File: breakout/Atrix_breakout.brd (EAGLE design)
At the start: 8.1 x 17.4 mm, 9 parts

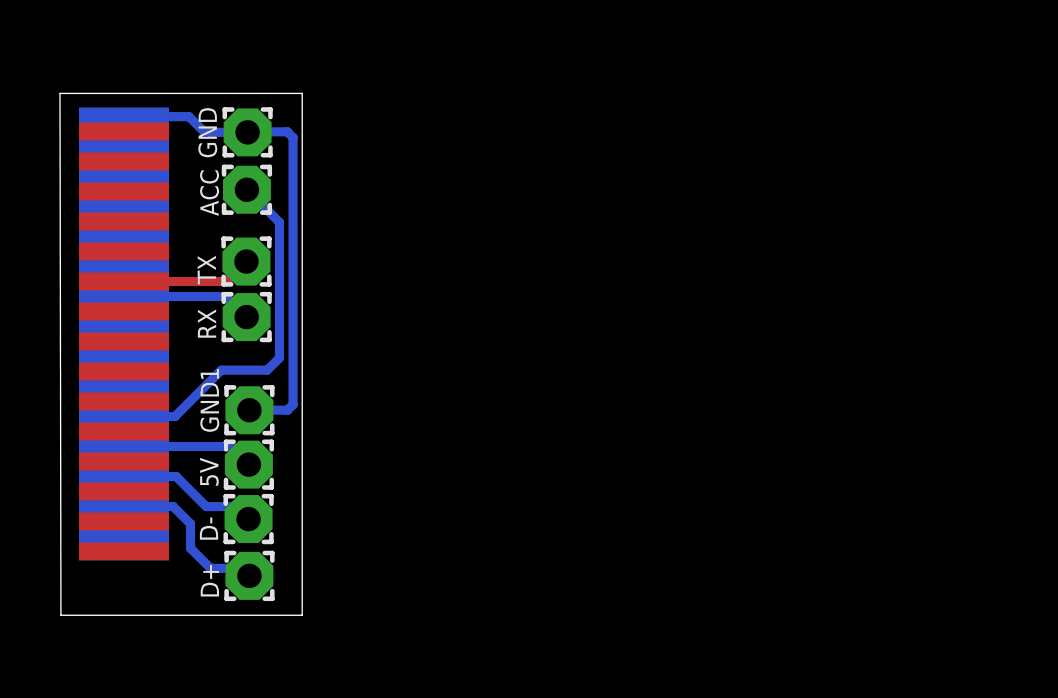
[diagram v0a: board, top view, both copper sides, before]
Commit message: Breakout updated to v1.0.1, improved board. See rev.txt
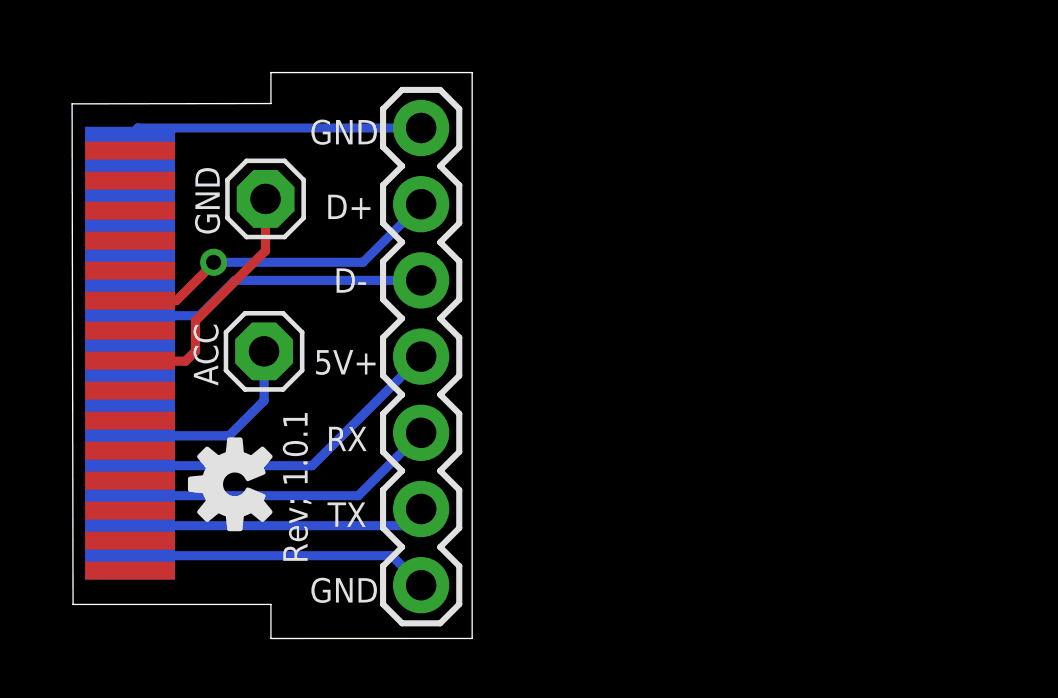
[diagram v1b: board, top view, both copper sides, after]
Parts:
- removed 5V, D+, D-, GND1, RX, TX: (no value), wirepad:1,6/0,8
- added JP1: (no value), SparkFun-Connectors:1X07
- added U$2: (no value), SparkFun-Aesthetics:OSHW-LOGO-S
- ACC, GND: device wirepad:1,6/0,8 -> adafruit:1X01
- moved ACC 5.42 mm to (4.77, 12.4)
- moved GND 2.30 mm to (4.82, 17.5)
- moved U$1 0.67 mm to (0.30, 12.1)
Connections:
- net N$2 renamed ACC
- removed net N$3: D-.1, U$1.25
- removed net N$4: D+.1, U$1.27
- removed net N$6: RX.1, U$1.13
- removed net N$7: TX.1, U$1.12
- removed net N$8: 5V.1, U$1.23
- new net 5V+: JP1.4, U$1.23
- new net ACC_GROUND: GND.1, U$1.16
- new net D+: JP1.2, U$1.27
- new net D-: JP1.3, U$1.25
- new net RX: JP1.5, U$1.13
- new net TX: JP1.6, U$1.12
- new net USB_GND: JP1.1, U$1.29
- net GND: now also JP1.7; no longer GND.1, GND1.1
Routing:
- net 5V+: track 0.00 -> 11.2 mm
- net TX: track 0.00 -> 11.1 mm, vias 0 -> 1
- net D-: track 0.00 -> 10.6 mm
- net RX: track 0.00 -> 10.2 mm
- net USB_GND: track 0.00 -> 10.1 mm
- net D+: track 0.00 -> 9.93 mm
- net ACC_GROUND: track 0.00 -> 8.37 mm
- net GND: track 16.4 -> 9.81 mm
- net N$4: track 5.62 -> 0.00 mm
- net ACC: track 12.0 -> 6.60 mm
- net N$3: track 4.74 -> 0.00 mm
- net N$8: track 4.41 -> 0.00 mm
- net N$6: track 4.37 -> 0.00 mm
- net N$7: track 4.36 -> 0.00 mm
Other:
- board size 8.1 x 17.4 mm -> 13.3 x 18.9 mm
- board text added: "5V+"
- board text added: "D+"
- board text added: "D-"
- board text added: "GND"
- board text added: "RX"
- board text added: "Rev; 1.0.1"
- board text added: "TX"

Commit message: Rev v1.0.2r2
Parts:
- removed ACC, GND: (no value), adafruit:1X01
- added R1: (no value), eagle-ltspice:0207/10
- added U$3: USB-MINIB-5PIN, SparkFun-Connectors:USB-MINIB
- JP1: device SparkFun-Connectors:1X07 -> con-amp-quick:03P
- moved U$2 18.2 mm to (21.3, 12.8)
- moved JP1 9.89 mm to (11.9, 14.3)
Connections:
- net 5V+: now also U$3.VBUS; no longer JP1.4
- net ACC: now also R1.2; no longer ACC.1
- net ACC_GROUND: now also R1.1; no longer GND.1
- net D+: now also U$3.D+; no longer JP1.2
- net D-: now also U$3.D-; no longer JP1.3
- net GND: now also JP1.3; no longer JP1.7
- net RX: now also JP1.1; no longer JP1.5
- net TX: now also JP1.2; no longer JP1.6
- net USB_GND: now also U$3.GND; no longer JP1.1
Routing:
- net D+: track 9.93 -> 22.6 mm
- net USB_GND: track 10.1 -> 22.3 mm
- net ACC_GROUND: track 8.37 -> 20.4 mm
- net D-: track 10.6 -> 22.5 mm
- net ACC: track 6.60 -> 17.9 mm, vias 0 -> 1
- net 5V+: track 11.2 -> 22.4 mm
- net GND: track 9.81 -> 12.7 mm
- net RX: track 10.2 -> 12.3 mm
- net TX: track 11.1 -> 11.7 mm, vias 1 -> 0
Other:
- board size 13.3 x 18.9 mm -> 30.8 x 16.8 mm
- board text added: "1"
- board text added: "29SQ-LRDW-TKJK"
- board text added: "470 Ohm"
- board text added: "v1.0.2r2"
- board text added: "~ haifisch greetz to musclenerd, notjonseals, herpes, frankie, p0k, & posix."
- board text removed: "5V+"
- board text removed: "D+"
- board text removed: "D-"
- board text removed: "Rev; 1.0.1"
